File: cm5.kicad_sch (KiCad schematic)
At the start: 14 parts, among them J2 CM5_1-100_3mm-stack, J3 CM5_101-200_3mm-stack, J4 JST_SH_1x3_BM03B-SRSS-TB-LF-SN

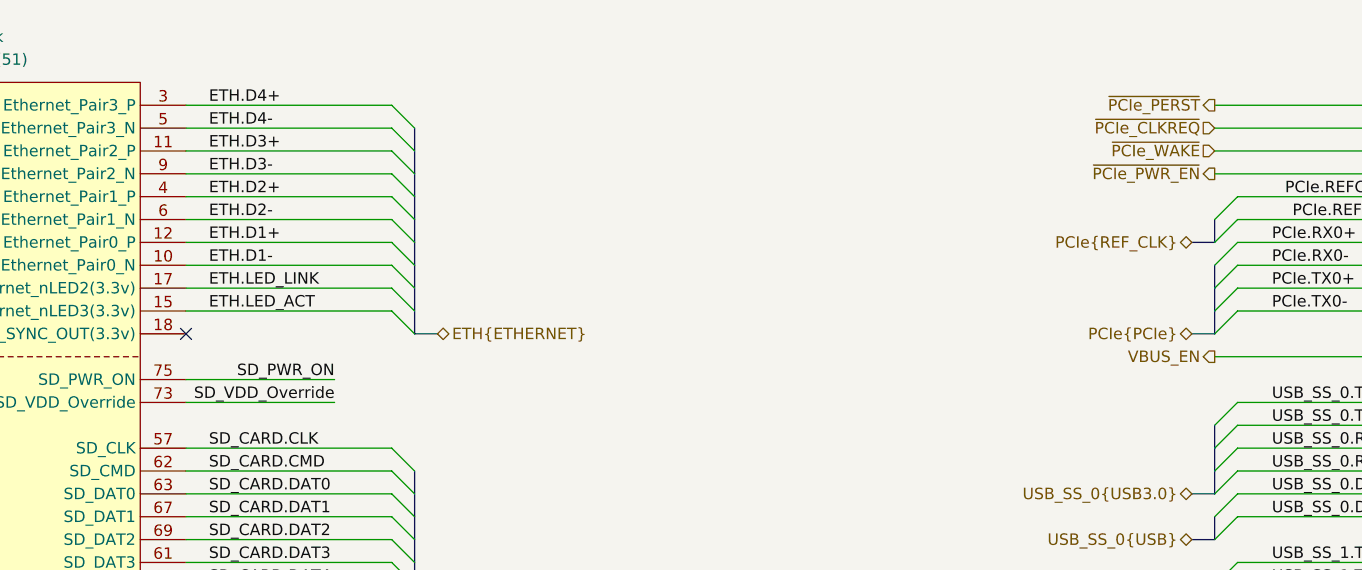
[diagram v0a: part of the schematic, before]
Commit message: [#1] WIP: Refactor schematic
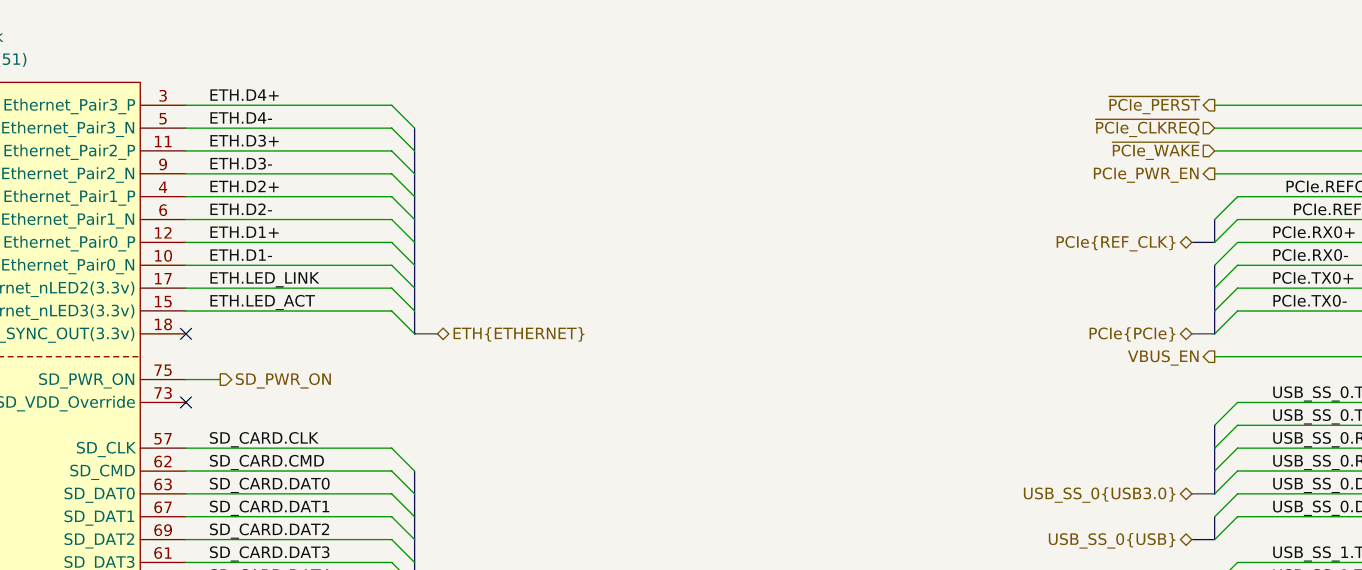
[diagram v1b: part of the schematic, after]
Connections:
- net SD_VDD_Override: no longer names the net of J2.73 (SD_VDD_Override)
- net ~{PCIe_PWR_EN} renamed PCIe_PWR_EN
- no-connect marks 2 -> 3
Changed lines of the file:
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@@
 		(at 127 113.03)
 	)
+	(no_connect
+		(at 127 120.65)
+	)
 	(bus_entry
 		(at 241.3 151.13)
@@
 		)
 	)
+	(wire
+		(pts
+			(xy 130.81 118.11) (xy 127 118.11)
+		)
+		(stroke
+			(width 0)
+			(type default)
+		)
+	)
 	(bus
 		(pts
@@
 	(wire
 		(pts
-			(xy 143.51 118.11) (xy 127 118.11)
-		)
-		(stroke
-			(width 0)
-			(type default)
-		)
-	)
-	(wire
-		(pts
 			(xy 86.36 251.46) (xy 97.79 251.46)
 		)
@@
 		)
 	)
-	(wire
-		(pts
-			(xy 143.51 120.65) (xy 127 120.65)
-		)
-		(stroke
-			(width 0)
-			(type default)
-		)
-	)
 	(bus
 		(pts
@@
 		)
 	)
-	(label "SD_PWR_ON"
-		(at 143.51 118.11 180)
-		(effects
-			(font
-				(size 1.27 1.27)
-			)
-			(justify right bottom)
-		)
-	)
 	(label "MIPI_1.D2-"
 		(at 326.39 128.27 0)
@@
 		)
 	)
-	(label "SD_VDD_Override"
-		(at 143.51 120.65 180)
-		(effects
-			(font
-				(size 1.27 1.27)
-			)
-			(justify right bottom)
-		)
-	)
 	(label "UART2_TX"
 		(at 50.8 95.25 0)
@@
 		)
 	)
-	(hierarchical_label "~{PCIe_PWR_EN}"
+	(hierarchical_label "PCIe_PWR_EN"
 		(shape output)
 		(at 241.3 95.25 180)
@@
 		)
 	)
+	(hierarchical_label "SD_PWR_ON"
+		(shape output)
+		(at 130.81 118.11 0)
+		(effects
+			(font
+				(size 1.27 1.27)
+			)
+			(justify left)
+		)
+	)
 	(hierarchical_label "~{PCIe_PERST}"
 		(shape output)
@@
 		(polyline
 			(pts
-				(xy 171.45 85.09) (xy 171.45 115.57) (xy 149.86 115.57) (xy 149.86 85.09)
+				(xy 243.84 114.3) (xy 217.17 114.3) (xy 217.17 96.52) (xy 243.84 96.52)
 			)
 			(stroke
@@
 		(polyline
 			(pts
-				(xy 243.84 114.3) (xy 217.17 114.3) (xy 217.17 96.52) (xy 243.84 96.52)
+				(xy 171.45 123.19) (xy 171.45 153.67) (xy 149.86 153.67) (xy 149.86 123.19)
 			)
 			(stroke
@@
 		(polyline
 			(pts
-				(xy 171.45 123.19) (xy 171.45 153.67) (xy 149.86 153.67) (xy 149.86 123.19)
+				(xy 243.84 162.56) (xy 217.17 162.56) (xy 217.17 119.38) (xy 243.84 119.38)
 			)
 			(stroke
@@
 		(polyline
 			(pts
-				(xy 243.84 162.56) (xy 217.17 162.56) (xy 217.17 119.38) (xy 243.84 119.38)
+				(xy 171.45 85.09) (xy 171.45 115.57) (xy 149.86 115.57) (xy 149.86 85.09)
 			)
 			(stroke

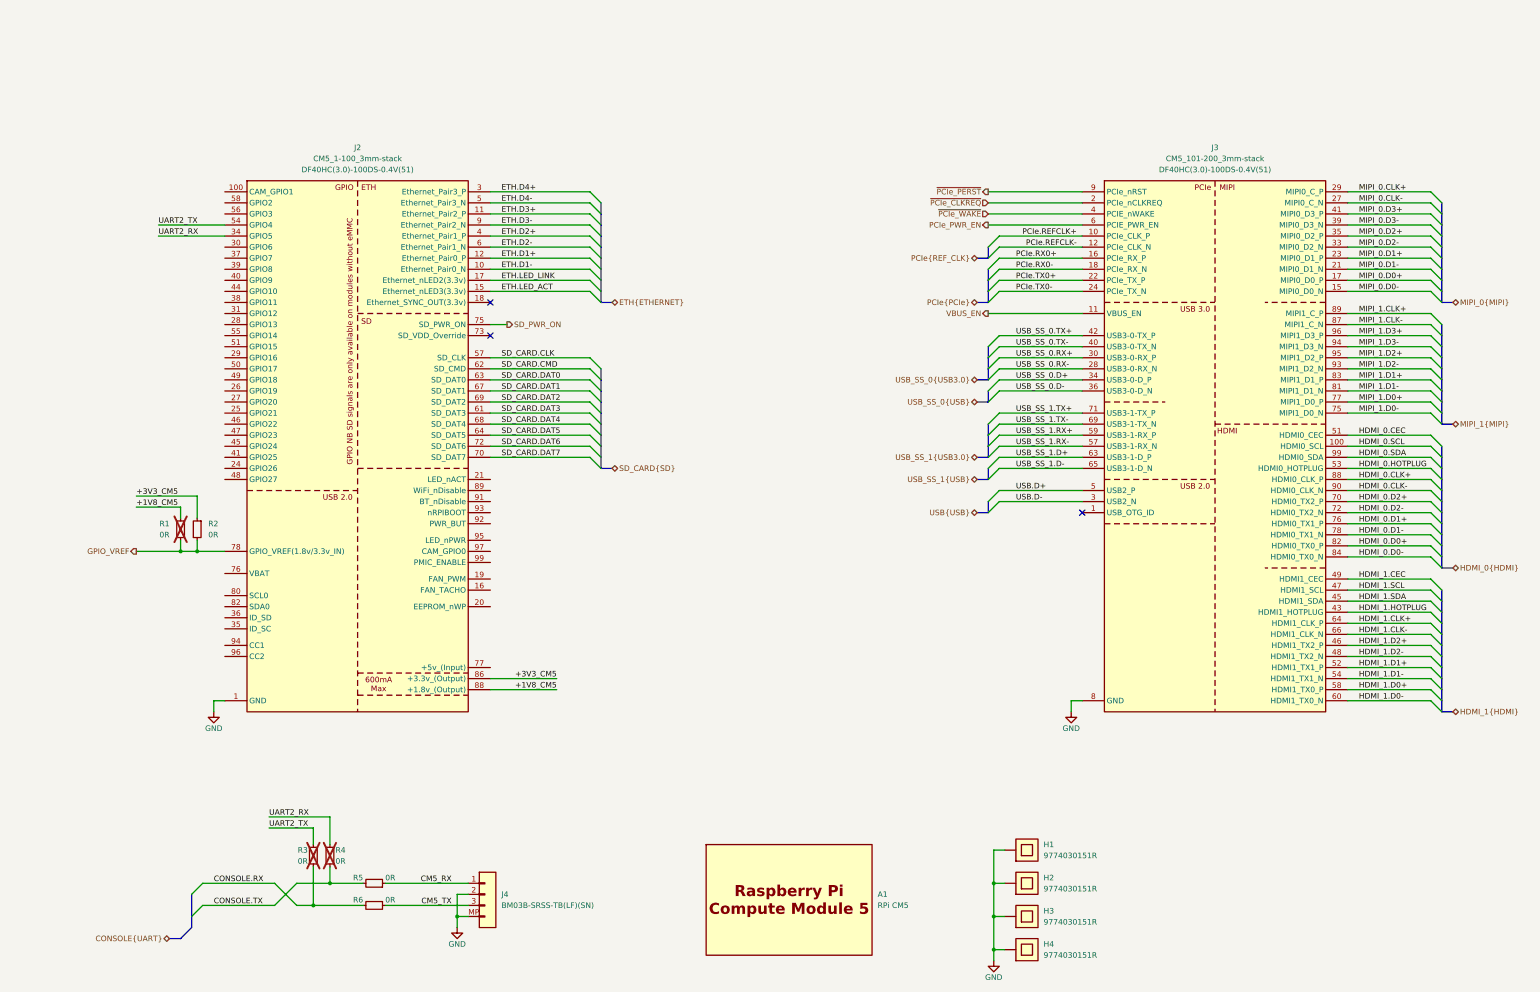
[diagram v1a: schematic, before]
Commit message: [#1] WIP: Refactor schematic
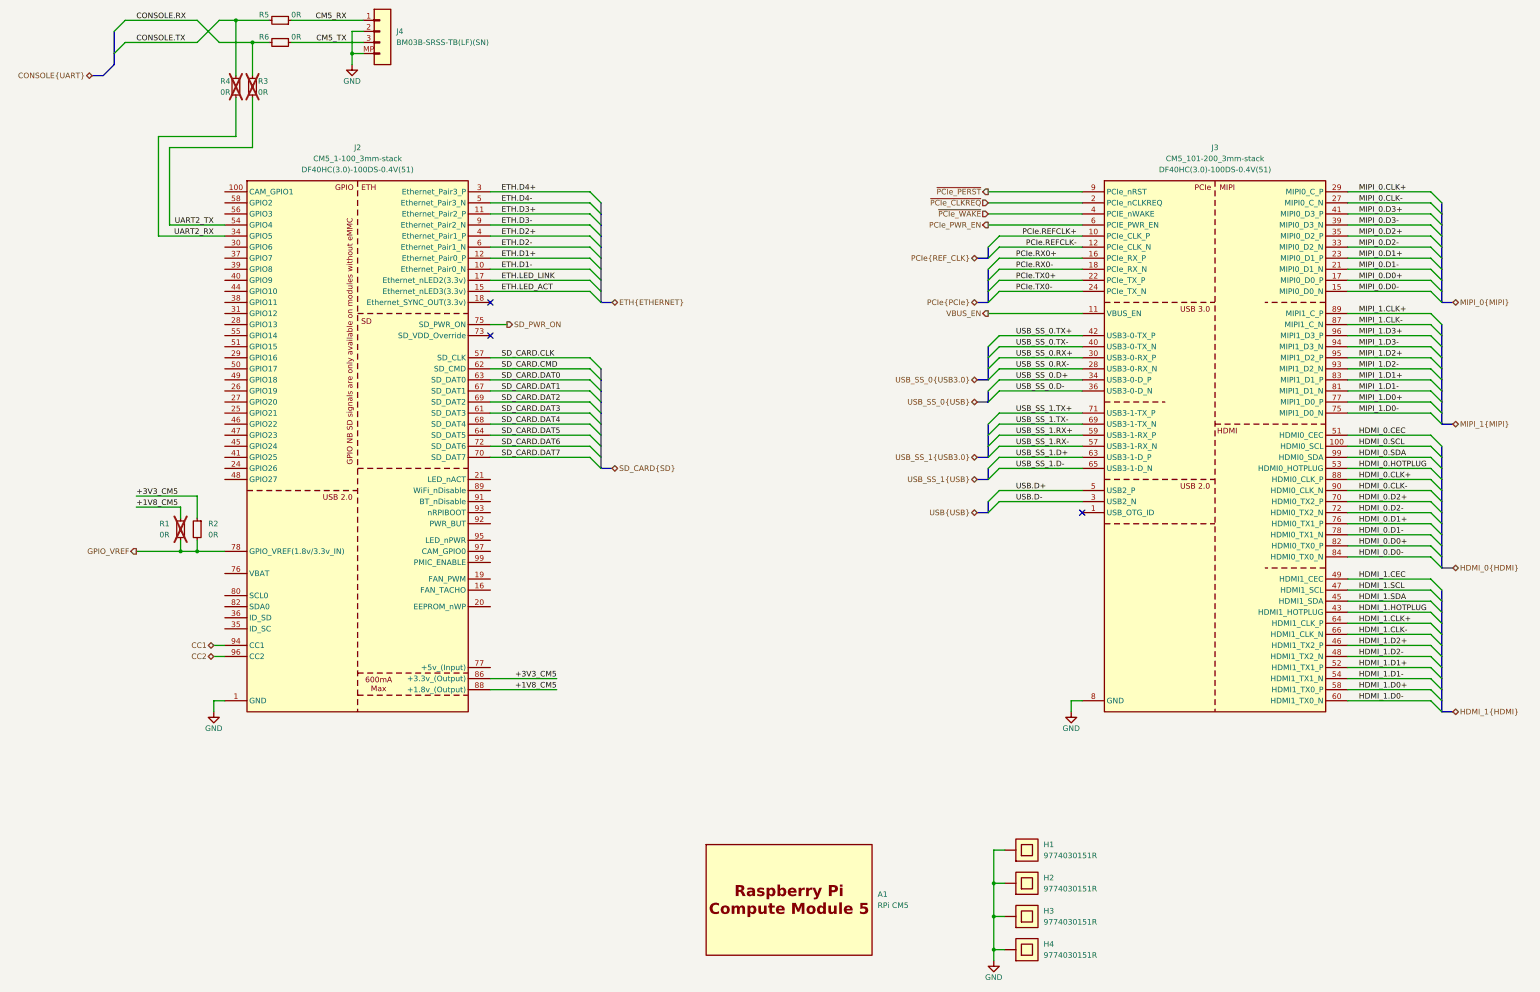
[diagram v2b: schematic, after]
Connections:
- net CONSOLE.RX: now also R3.2; no longer R3.1
- net CONSOLE.TX: now also R4.2; no longer R4.1
- net UART2_RX: now also R4.1; no longer R4.2
- net UART2_TX: now also R3.1; no longer R3.2
- net CC1: now reaches J2.94 (CC1)
- net CC2: now reaches J2.96 (CC2)
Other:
- moved on the sheet: J4, R3, R4, R5, R6

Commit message: [#1] Update CM5 connectors symbols, connect its misc pins
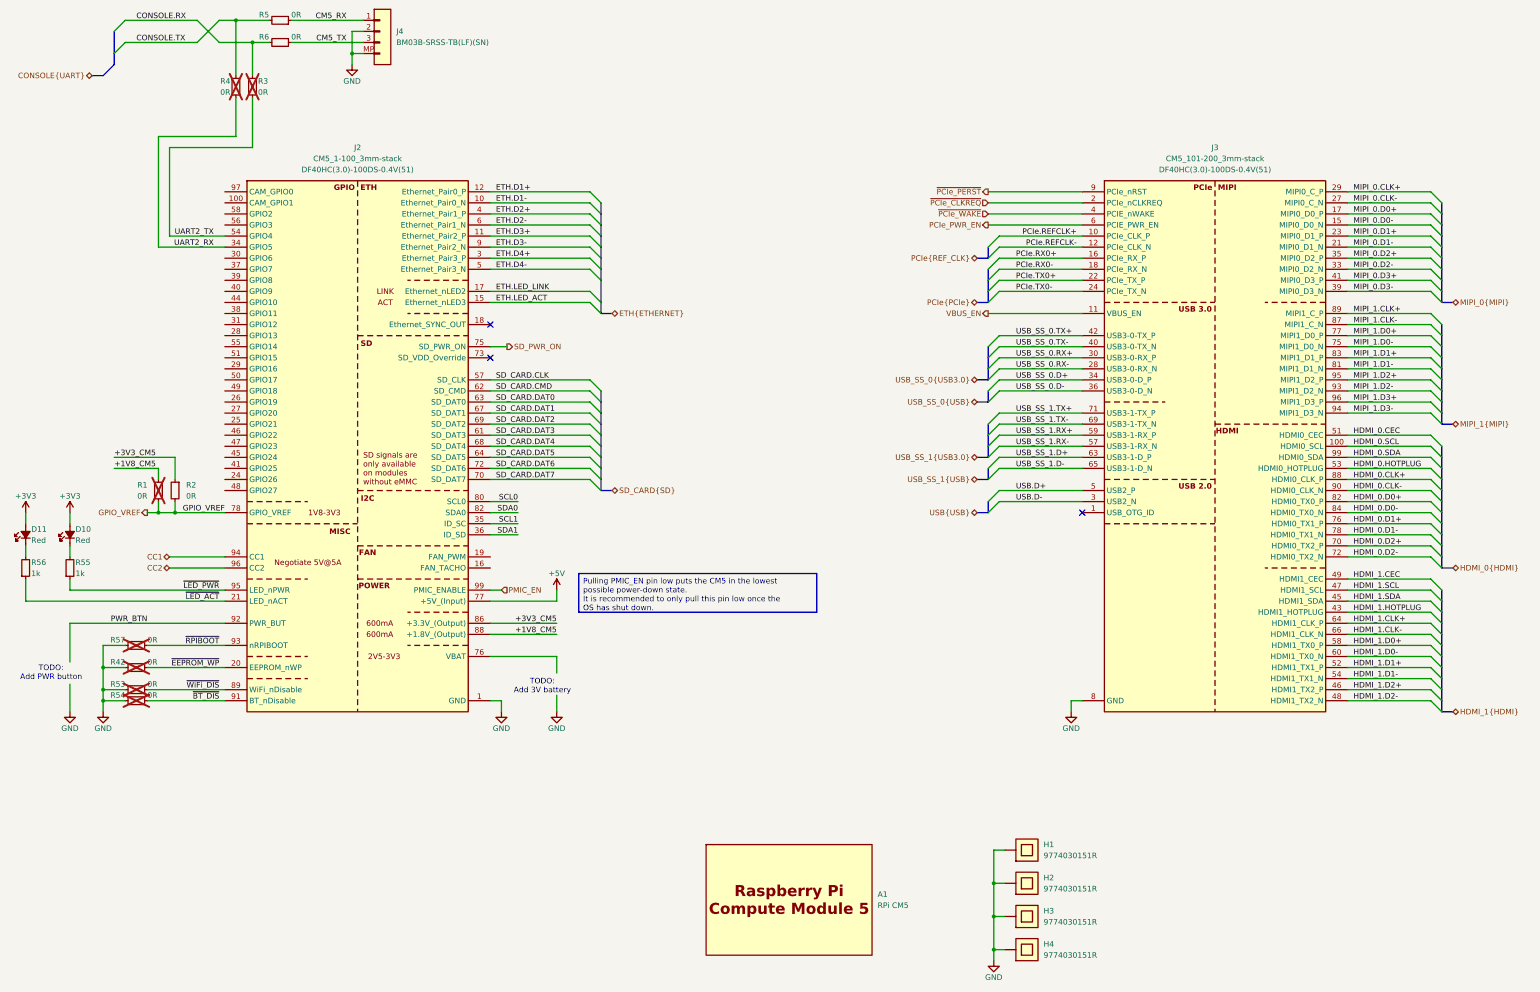
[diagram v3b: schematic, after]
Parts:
- added D10, D11: LED-R-0603_KT-0603R, DW-footprints:LED_0603_1608Metric_R, symbol DW-diodes:LED-R-0603_KT-0603R
- added R42, R53, R54, R57: R-0R-0402, DW-footprints:R_0402_1005Metric, symbol DW-resistors:R-0R-0402
- added R55, R56: R-1k-0402, DW-footprints:R_0402_1005Metric, symbol DW-resistors:R-1k-0402
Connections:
- net GND: now also R42.1, R53.1, R54.1, R57.1
- net ~{EEPROM_WP}: now reaches J2.20 (EEPROM_nWP)
- net ~{EEPROM_WP}: now also R42.2
- net ~{LED_ACT}: now reaches J2.21 (LED_nACT)
- net ~{LED_ACT}: now also R56.1
- net SCL1: now reaches J2.35 (ID_SC)
- net SDA1: now reaches J2.36 (ID_SD)
- net SCL0: now reaches J2.80 (SCL0)
- net SDA0: now reaches J2.82 (SDA0)
- net ~{WiFi_DIS}: now reaches J2.89 (WiFi_nDisable)
- net ~{WiFi_DIS}: now also R53.2
- net ~{BT_DIS}: now reaches J2.91 (BT_nDisable)
- net ~{BT_DIS}: now also R54.2
- net PWR_BTN: now reaches J2.92 (PWR_BUT)
- net ~{RPIBOOT}: now reaches J2.93 (nRPIBOOT)
- net ~{RPIBOOT}: now also R57.2
- net ~{LED_PWR}: now reaches J2.95 (LED_nPWR)
- net ~{LED_PWR}: now also R55.1
- net PMIC_EN: now reaches J2.99 (PMIC_ENABLE)
- net +5v_(Input) renamed +5V
- new net: D11.1 (C), R56.2
- new net: D10.1 (C), R55.2
- new net +3V3: D10.2 (A), D11.2 (A)
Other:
- note added: "TODO: Add 3V battery"
- note added: "TODO: Add PWR button"
- moved on the sheet: R1, R2

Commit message: [#1] Add cooling fan connector
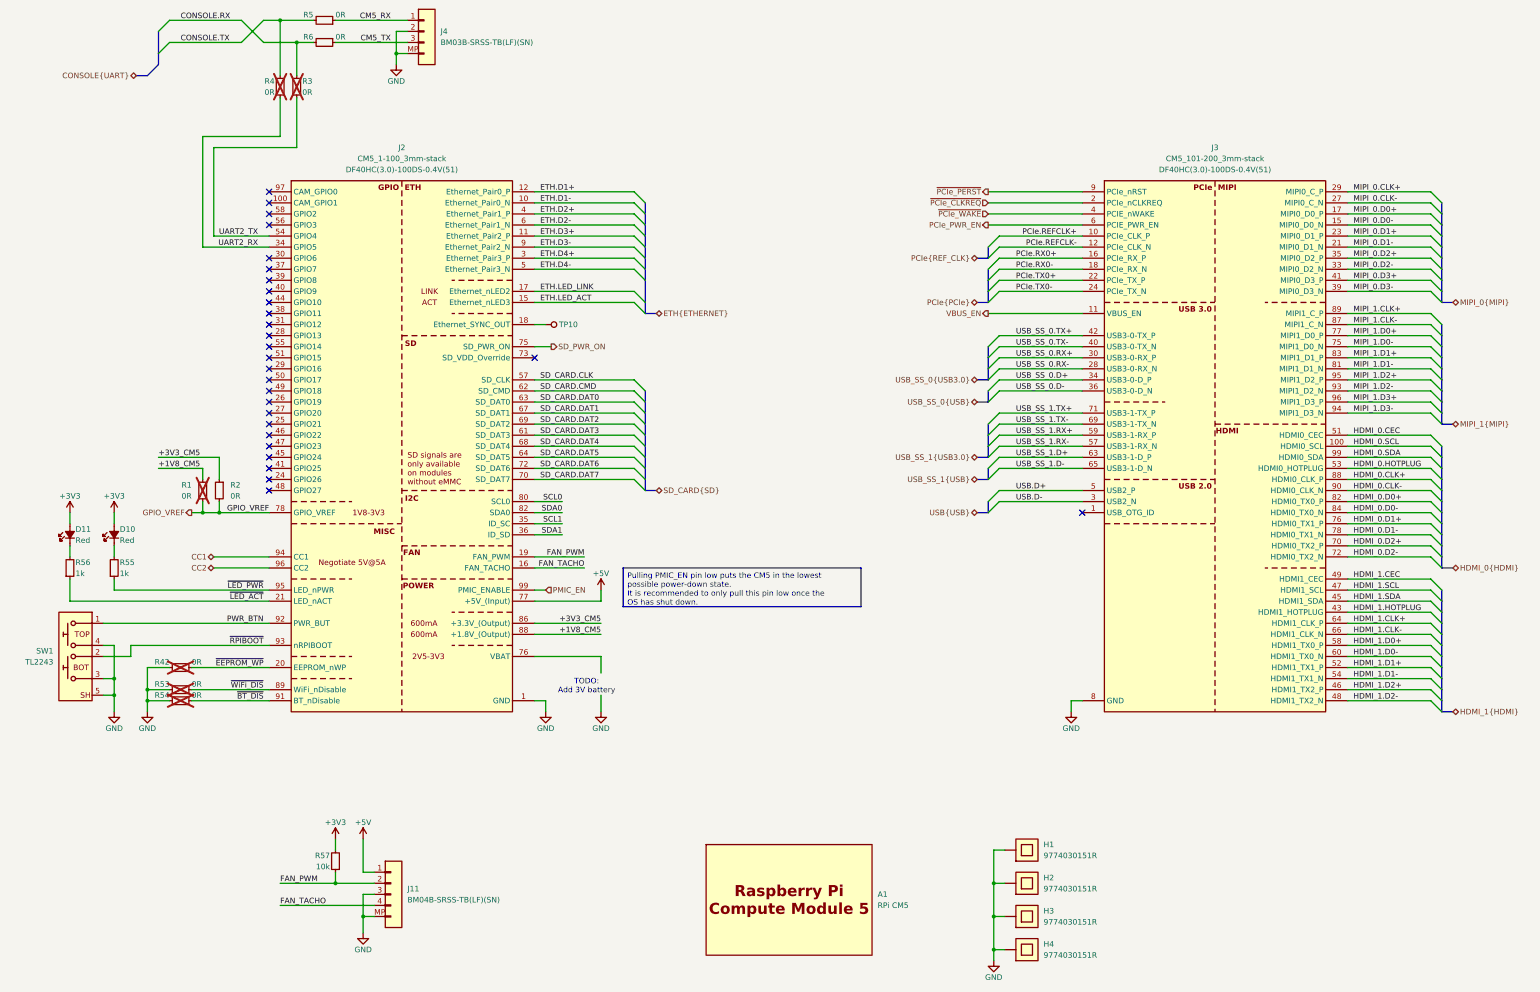
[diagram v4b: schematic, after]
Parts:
- removed R57: R-0R-0402, DW-footprints:R_0402_1005Metric, symbol DW-resistors:R-0R-0402
- added J11: JST_SH_1x4_BM04B-SRSS-TB-LF-SN, DW-footprints:Conn_JST_SH_1x4_BM04B-SRSS-TB, symbol DW-connectors:JST_SH_1x4_BM04B-SRSS-TB-LF-SN
- added R57: R-10k-0402, DW-footprints:R_0402_1005Metric, symbol DW-resistors:R-10k-0402
- added SW1: SW_TL2243, DW-footprints:SW_TL2243, symbol DW-mechanical:SW_TL2243
- added TP10: TP_SMD_0.75mm, DW-footprints:TP_SMD_0.75mm, symbol DW-test-points:TP_SMD_0.75mm
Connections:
- net +3V3: now also R57.2
- net +5V: now also J11.1
- net GND: now also J11.3, J11.MP, SW1.3 (BOTTOM_SW_2), SW1.4 (BOTTOM_SW_2), SW1.5 (SH), SW1.6 (SH)
- net PWR_BTN: now also SW1.1 (BOTTOM_SW_1)
- net ~{RPIBOOT}: now also SW1.2 (BOTTOM_SW_1)
- net FAN_TACHO: now reaches J2.16 (FAN_TACHO)
- net FAN_TACHO: now also J11.4
- net at J2.18 (Ethernet_SYNC_OUT): now also TP10.1
- net FAN_PWM: now reaches J2.19 (FAN_PWM)
- net FAN_PWM: now also J11.2, R57.1
- no-connect marks 3 -> 28
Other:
- note removed: "TODO: Add PWR button"
- moved on the sheet: D10, D11, J2, J4, R1, R2, R3, R4, R42, R5, R53, R54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
